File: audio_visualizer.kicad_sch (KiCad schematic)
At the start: 4 parts

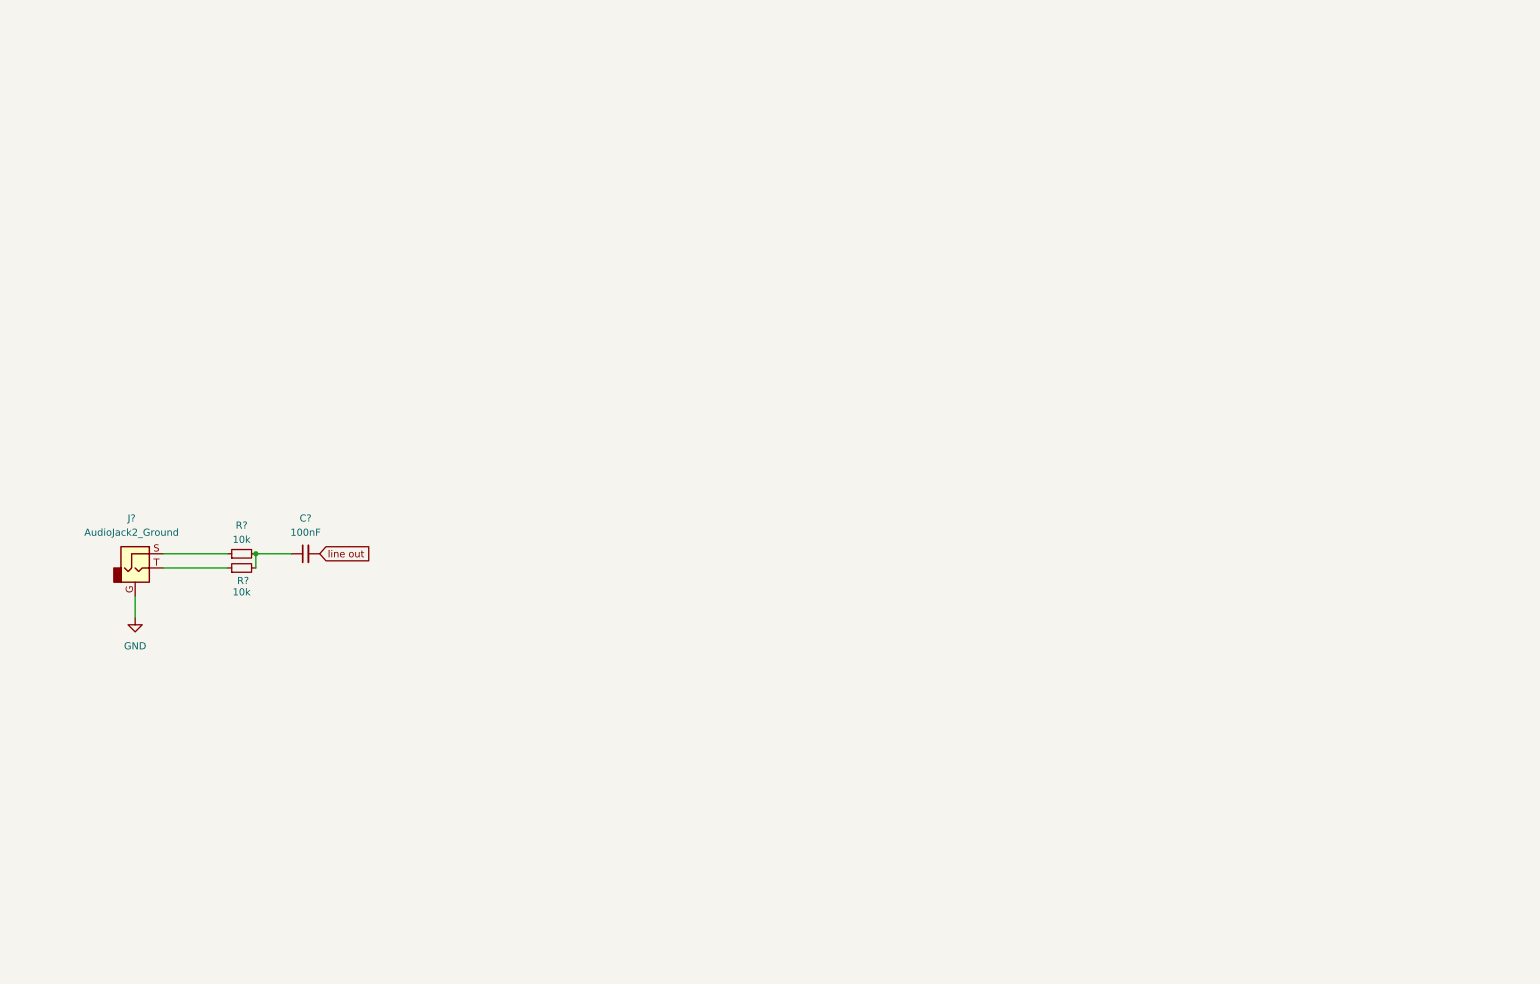
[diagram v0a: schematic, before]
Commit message: added mic and line in switch schematic
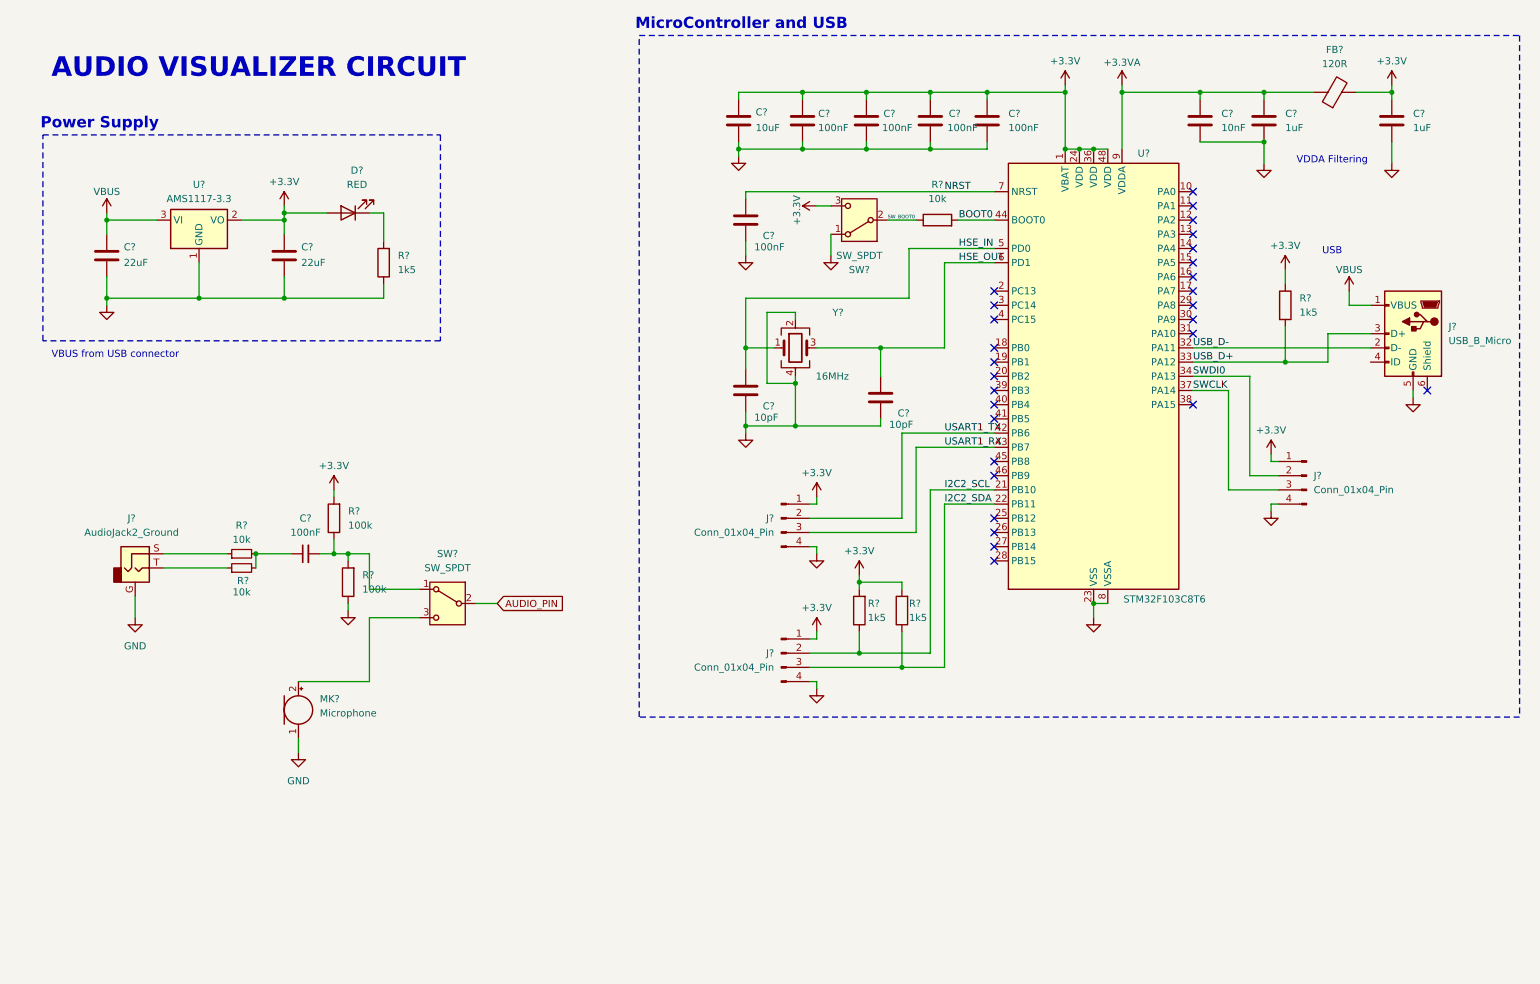
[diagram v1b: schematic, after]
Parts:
- added C? (x2): 10pF, symbol Device:C
- added C? (x5): 100nF, symbol Device:C
- added C?: 10nF, symbol Device:C
- added C? (x2): 22uF, symbol Device:C
- added C?: 10uF, symbol Device:C
- added C? (x2): 1uF, symbol Device:C
- added D?: RED, symbol Device:LED
- added FB?: 120R, symbol Device:FerriteBead
- added J? (x3): Conn_01x04_Pin, symbol Connector:Conn_01x04_Pin
- added J?: USB_B_Micro, symbol Connector:USB_B_Micro
- added MK?: Microphone, symbol Device:Microphone
- added R? (x4): 1k5, symbol Device:R
- added R? (x2): 100k, symbol Device:R
- added R?: 10k, symbol Device:R
- added SW? (x2): SW_SPDT, symbol Switch:SW_SPDT
- added U?: STM32F103C8T6, Package_QFP:LQFP-48_7x7mm_P0.5mm, symbol MCU_ST_STM32F1:STM32F103C8Tx
- added U?: AMS1117-3.3, Package_TO_SOT_SMD:SOT-223-3_TabPin2, symbol Regulator_Linear:AMS1117-3.3
- added Y?: 16MHz, symbol Device:Crystal_GND24
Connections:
- net GND: now also C?.2, C?.2, C?.2, C?.2, C?.2, C?.2, C?.2, C?.2, C?.2, C?.2, C?.2, C?.2, C?.2, J?.4 (Pin_4), J?.4 (Pin_4), J?.4 (Pin_4), J?.5 (GND), MK?.1 (-), R?.1, R?.1, SW?.1 (A), U?.1 (GND), U?.23 (VSS), U?.35 (VSS), U?.47 (VSS), U?.8 (VSSA), Y?.2, Y?.4
- net line out: no longer names the net of C?.2
- net line out: now also R?.1, R?.2, SW?.1 (A)
- new net: D?.1 (K), R?.2
- new net: MK?.2 (+), SW?.3 (C)
- new net +3.3V: C?.1, C?.1, C?.1, C?.1, C?.1, C?.1, C?.1, D?.2 (A), FB?.2, J?.1 (Pin_1), J?.1 (Pin_1), J?.1 (Pin_1), R?.1, R?.2, R?.2, R?.2, SW?.3 (C), U?.1 (VBAT), U?.2 (VO), U?.24 (VDD), U?.36 (VDD), U?.48 (VDD)
- new net +3.3VA: C?.1, C?.1, FB?.1, U?.9 (VDDA)
- new net AUDIO_PIN: SW?.2 (B)
- new net BOOT0: R?.2, U?.44 (BOOT0)
- new net HSE_IN: C?.1, U?.5 (PD0), Y?.1
- new net HSE_OUT: C?.1, U?.6 (PD1), Y?.3
- new net I2C2_SCL: J?.2 (Pin_2), R?.1, U?.21 (PB10)
- new net I2C2_SDA: J?.3 (Pin_3), R?.1, U?.22 (PB11)
- new net NRST: C?.1, U?.7 (NRST)
- new net SWCLK: J?.3 (Pin_3), U?.37 (PA14)
- new net SWDI0: J?.2 (Pin_2), U?.34 (PA13)
- new net SW_BOOT0: R?.1, SW?.2 (B)
- new net USART1_RX: J?.3 (Pin_3), U?.43 (PB7)
- new net USART1_TX: J?.2 (Pin_2), U?.42 (PB6)
- new net USB_D+: J?.3 (D+), R?.2, U?.33 (PA12)
- new net USB_D-: J?.2 (D-), U?.32 (PA11)
- new net VBUS: C?.1, J?.1 (VBUS), U?.3 (VI)
- no-connect marks 0 -> 28
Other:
- note added: "AUDIO VISUALIZER CIRCUIT"
- note added: "MicroController and USB"
- note added: "Power Supply"
- note added: "USB"
- note added: "VBUS from USB connector"
- note added: "VDDA Filtering"
- title: (none) -> Audio Visualizer PCB

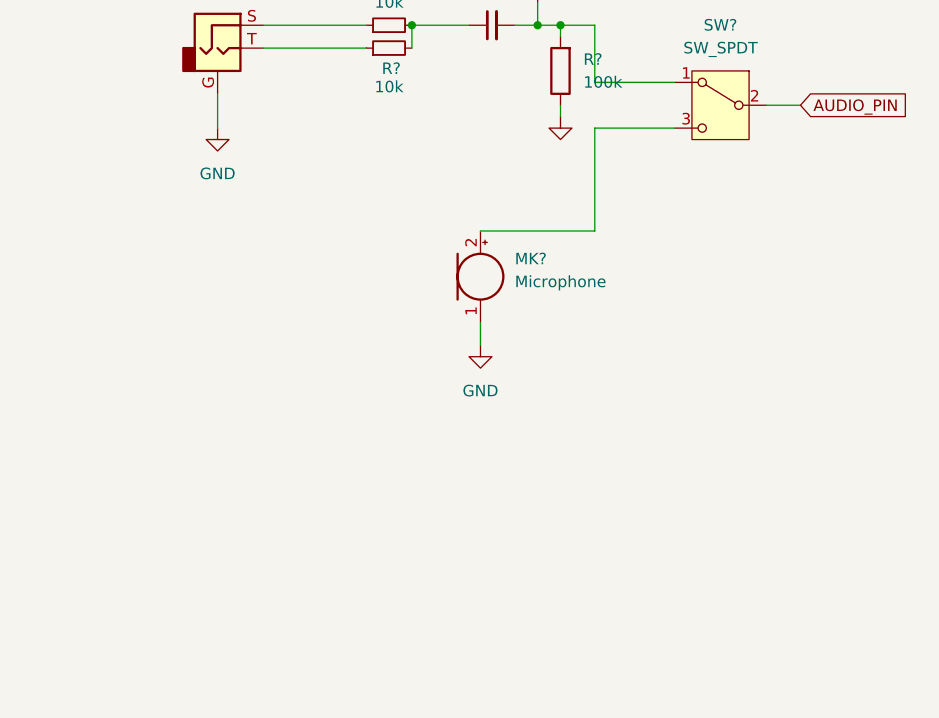
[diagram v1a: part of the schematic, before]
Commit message: added active bandpass filter to mic input
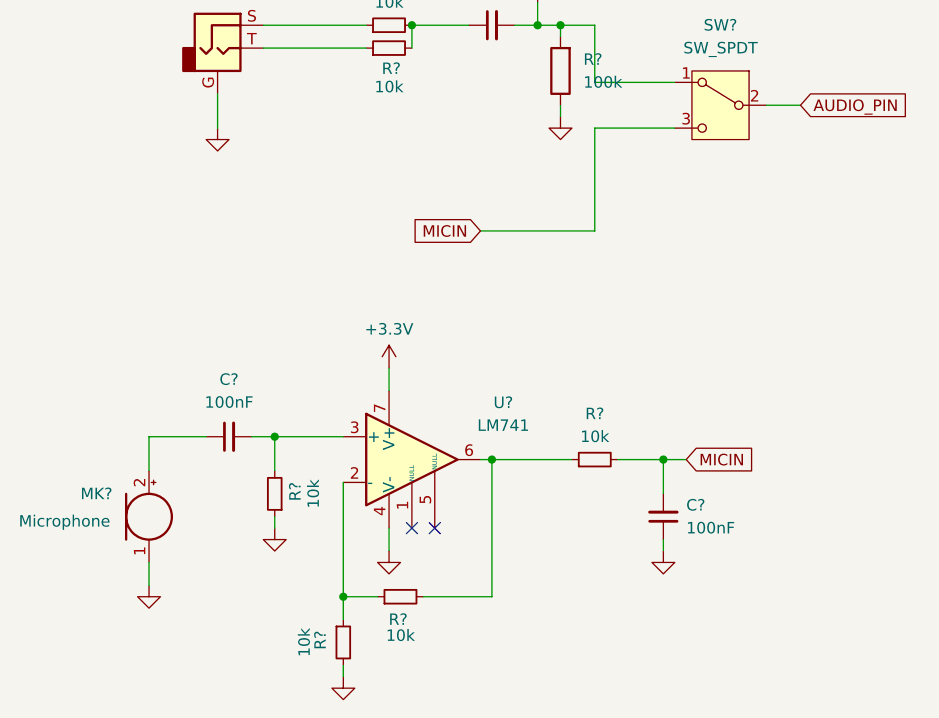
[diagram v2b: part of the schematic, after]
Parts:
- added C? (x2): 100nF, symbol Device:C_Small
- added R? (x4): 10k, symbol Device:R_Small
- added U?: LM741, symbol Amplifier_Operational:LM741
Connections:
- net +3.3V: now also U?.7 (V+)
- net GND: now also C?.1, R?.1, R?.2, U?.4 (V-)
- net at MK?.2 (+): now also C?.1; no longer SW?.3 (C)
- new net: R?.1, R?.1, U?.2 (-)
- new net: C?.2, R?.2, U?.3 (+)
- new net: R?.1, R?.2, U?.6
- new net MICIN: C?.2, R?.2, SW?.3 (C)
- no-connect marks 28 -> 30
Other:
- moved on the sheet: MK?
